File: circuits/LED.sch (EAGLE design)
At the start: 17 parts, among them X1 2516-

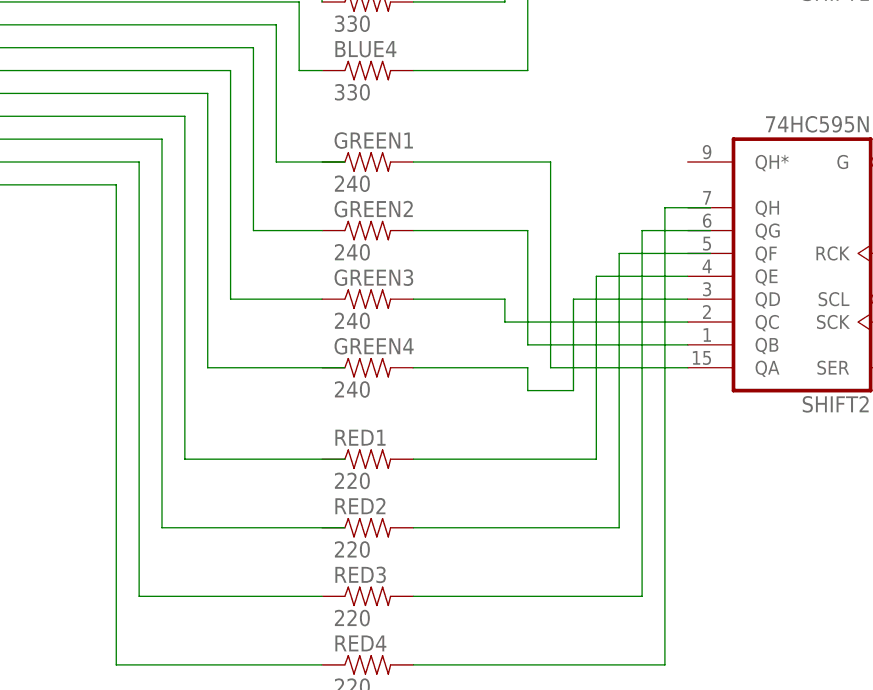
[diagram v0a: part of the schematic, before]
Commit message: Fix schematic & lay out board
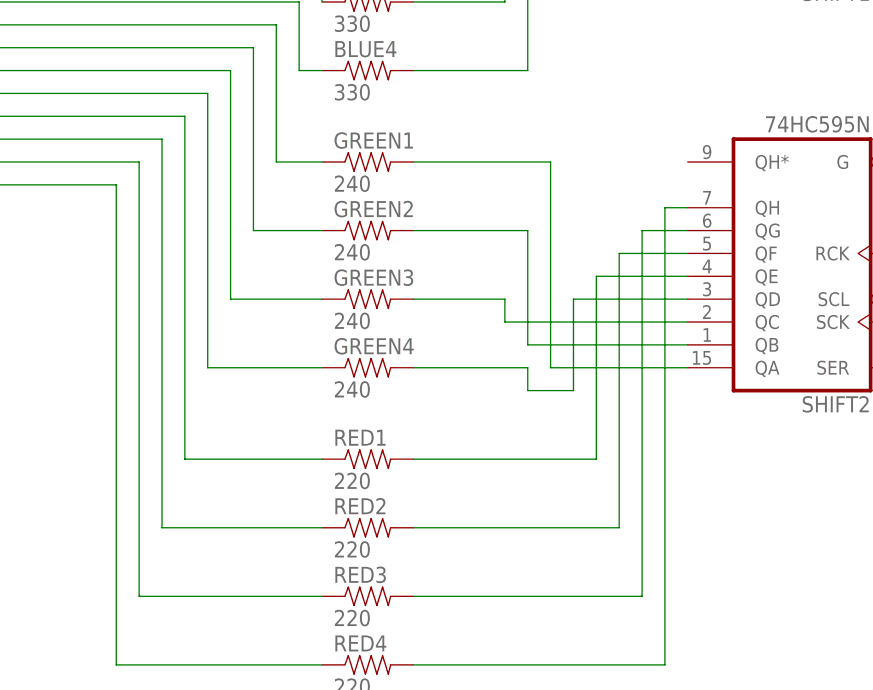
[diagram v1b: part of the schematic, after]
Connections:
- net N$13: now also GREEN1.1
- net N$16: now also GREEN4.1
- net N$17: now also RED1.1
- net N$18: now also RED2.1
- net N$26: now also SHIFT2A.QF
- net N$27: now also SHIFT2A.QG
- net N$28: now also SHIFT2A.QH
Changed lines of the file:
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@@
 <wire x1="45.72" y1="116.84" x2="114.3" y2="116.84" width="0.1524" layer="91"/>
 <wire x1="114.3" y1="116.84" x2="114.3" y2="101.6" width="0.1524" layer="91"/>
-<wire x1="114.3" y1="101.6" x2="121.92" y2="101.6" width="0.1524" layer="91"/>
+<pinref part="GREEN1" gate="G$1" pin="1"/>
+<wire x1="114.3" y1="101.6" x2="119.38" y2="101.6" width="0.1524" layer="91"/>
 </segment>
 </net>
@@
 <wire x1="45.72" y1="109.22" x2="106.68" y2="109.22" width="0.1524" layer="91"/>
 <wire x1="106.68" y1="109.22" x2="106.68" y2="78.74" width="0.1524" layer="91"/>
-<wire x1="106.68" y1="78.74" x2="121.92" y2="78.74" width="0.1524" layer="91"/>
+<pinref part="GREEN4" gate="G$1" pin="1"/>
+<wire x1="106.68" y1="78.74" x2="119.38" y2="78.74" width="0.1524" layer="91"/>
 </segment>
 </net>
@@
 <wire x1="45.72" y1="106.68" x2="104.14" y2="106.68" width="0.1524" layer="91"/>
 <wire x1="104.14" y1="106.68" x2="104.14" y2="68.58" width="0.1524" layer="91"/>
-<wire x1="104.14" y1="68.58" x2="121.92" y2="68.58" width="0.1524" layer="91"/>
+<pinref part="RED1" gate="G$1" pin="1"/>
+<wire x1="104.14" y1="68.58" x2="119.38" y2="68.58" width="0.1524" layer="91"/>
 </segment>
 </net>
@@
 <wire x1="45.72" y1="104.14" x2="101.6" y2="104.14" width="0.1524" layer="91"/>
 <wire x1="101.6" y1="104.14" x2="101.6" y2="60.96" width="0.1524" layer="91"/>
-<wire x1="101.6" y1="60.96" x2="121.92" y2="60.96" width="0.1524" layer="91"/>
+<pinref part="RED2" gate="G$1" pin="1"/>
+<wire x1="101.6" y1="60.96" x2="119.38" y2="60.96" width="0.1524" layer="91"/>
 </segment>
 </net>
@@
 <wire x1="129.54" y1="60.96" x2="152.4" y2="60.96" width="0.1524" layer="91"/>
 <wire x1="152.4" y1="60.96" x2="152.4" y2="91.44" width="0.1524" layer="91"/>
-<wire x1="152.4" y1="91.44" x2="162.56" y2="91.44" width="0.1524" layer="91"/>
+<pinref part="SHIFT2" gate="A" pin="QF"/>
+<wire x1="152.4" y1="91.44" x2="160.02" y2="91.44" width="0.1524" layer="91"/>
 </segment>
 </net>
@@
 <wire x1="129.54" y1="53.34" x2="154.94" y2="53.34" width="0.1524" layer="91"/>
 <wire x1="154.94" y1="53.34" x2="154.94" y2="93.98" width="0.1524" layer="91"/>
-<wire x1="154.94" y1="93.98" x2="162.56" y2="93.98" width="0.1524" layer="91"/>
+<pinref part="SHIFT2" gate="A" pin="QG"/>
+<wire x1="154.94" y1="93.98" x2="160.02" y2="93.98" width="0.1524" layer="91"/>
 </segment>
 </net>
@@
 <wire x1="129.54" y1="45.72" x2="157.48" y2="45.72" width="0.1524" layer="91"/>
 <wire x1="157.48" y1="45.72" x2="157.48" y2="96.52" width="0.1524" layer="91"/>
-<wire x1="157.48" y1="96.52" x2="162.56" y2="96.52" width="0.1524" layer="91"/>
+<pinref part="SHIFT2" gate="A" pin="QH"/>
+<wire x1="157.48" y1="96.52" x2="160.02" y2="96.52" width="0.1524" layer="91"/>
 </segment>
 </net>
